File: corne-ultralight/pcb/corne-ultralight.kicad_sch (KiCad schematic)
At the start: 110 parts, among them J2 OLED, J7 OLED, SW1 SW_PUSH, SW10 SW_PUSH, SW11 SW_PUSH, SW12 SW_PUSH, SW13 SW_PUSH, SW14 SW_PUSH, SW15 SW_PUSH, SW16 SW_PUSH, SW17 SW_PUSH, SW18 SW_PUSH, SW19 SW_PUSH, SW2 SW_PUSH, SW20 SW_PUSH, SW21 SW_PUSH, SW22 SW_PUSH, SW23 SW_PUSH, SW24 SW_PUSH, SW25 SW_PUSH, SW26 SW_PUSH, SW27 SW_PUSH, SW28 SW_PUSH, SW29 SW_PUSH, SW3 SW_PUSH, SW30 SW_PUSH, SW31 SW_PUSH, SW32 SW_PUSH, SW33 SW_PUSH, SW34 SW_PUSH, SW35 SW_PUSH, SW36 SW_PUSH, SW37 SW_PUSH, SW38 SW_PUSH, SW39 SW_PUSH, SW4 SW_PUSH, SW40 SW_PUSH, SW41 SW_PUSH, SW42 SW_PUSH, SW5 SW_PUSH, SW6 SW_PUSH, SW7 SW_PUSH, SW8 SW_PUSH, SW9 SW_PUSH, U1 ProMicro, U2 ProMicro

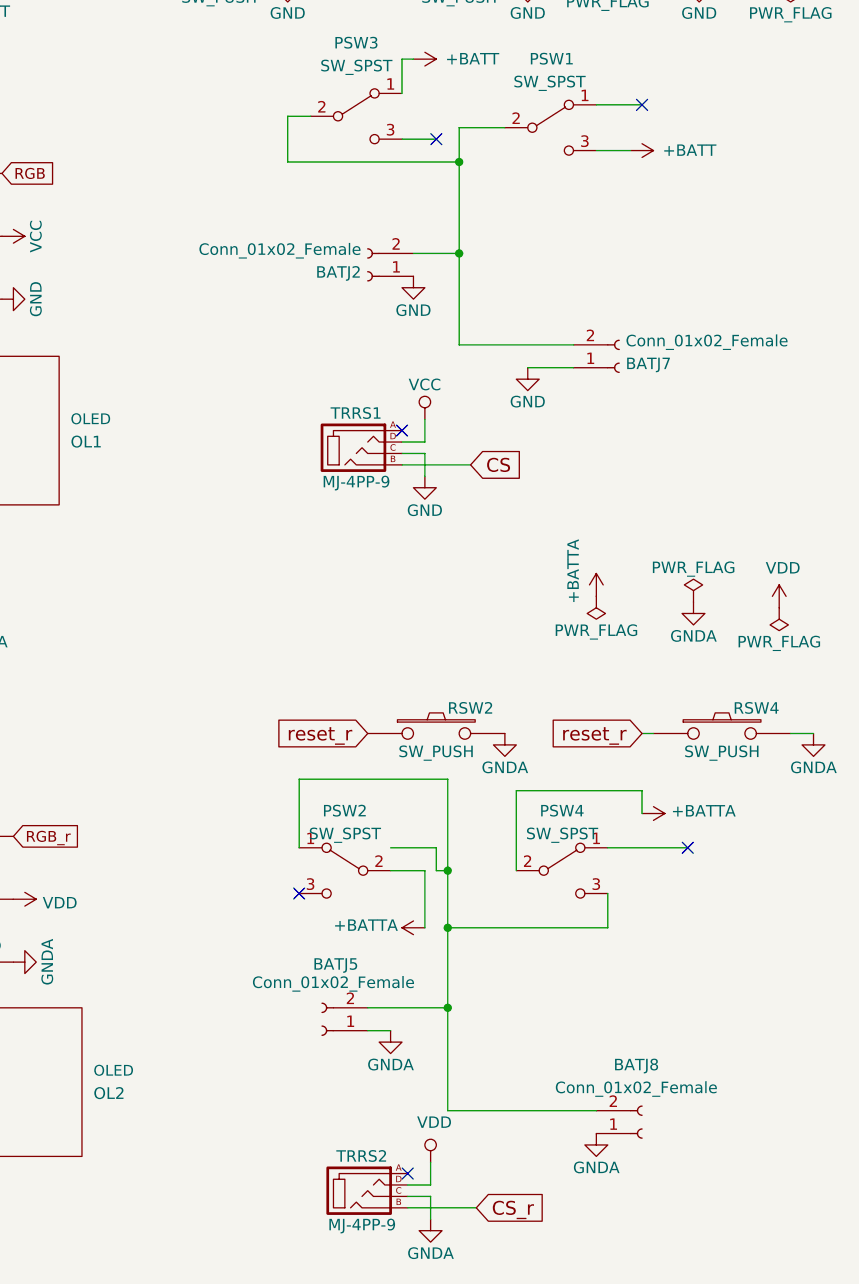
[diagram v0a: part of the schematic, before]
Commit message: Rerouting
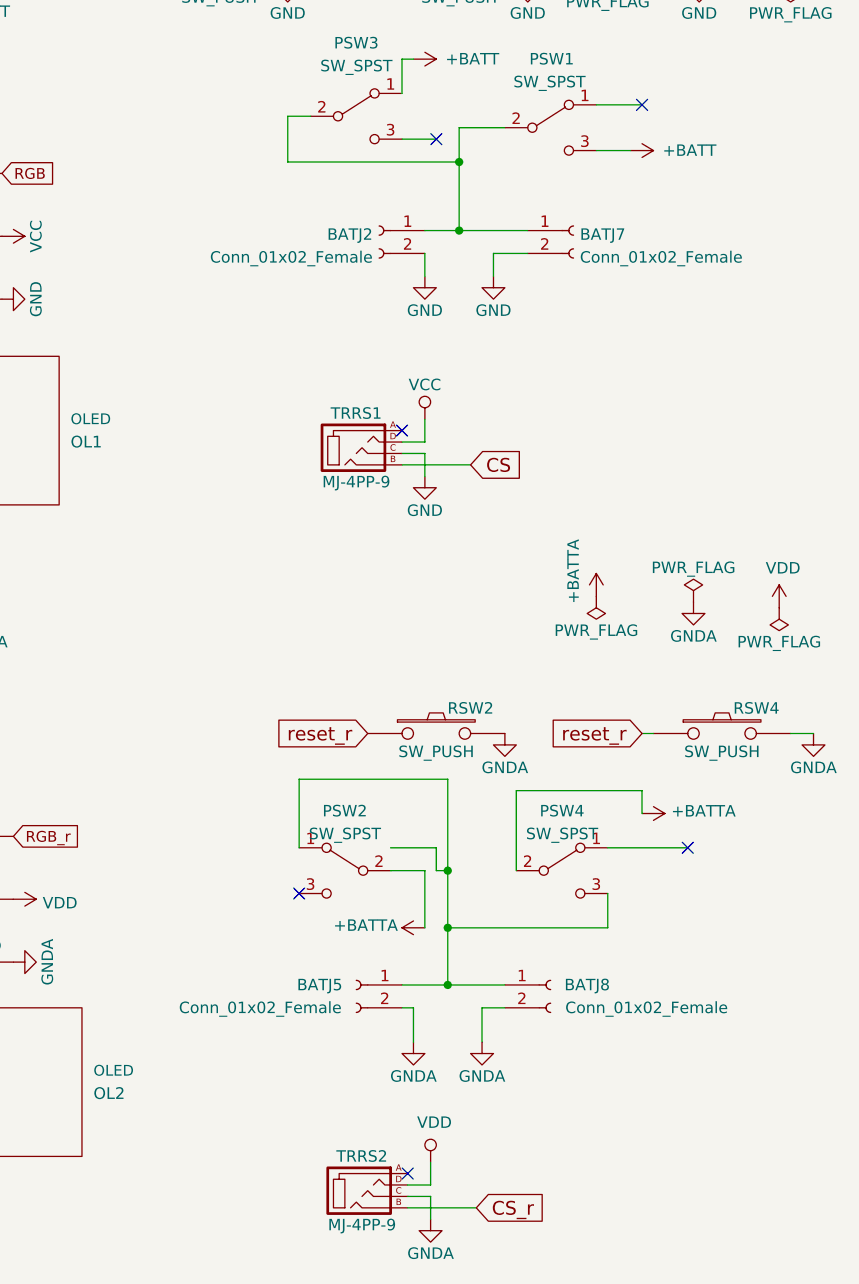
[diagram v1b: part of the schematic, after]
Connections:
- net GND: now also BATJ2.2 (Pin_2), BATJ7.2 (Pin_2); no longer BATJ2.1 (Pin_1), BATJ7.1 (Pin_1)
- net GNDA: now also BATJ5.2 (Pin_2), BATJ8.2 (Pin_2); no longer BATJ5.1 (Pin_1), BATJ8.1 (Pin_1)
- net at PSW2.1 (A), PSW4.3 (C): now also BATJ5.1 (Pin_1), BATJ8.1 (Pin_1); no longer BATJ5.2 (Pin_2), BATJ8.2 (Pin_2)
- net at PSW1.2 (B), PSW3.2 (B): now also BATJ2.1 (Pin_1), BATJ7.1 (Pin_1); no longer BATJ2.2 (Pin_2), BATJ7.2 (Pin_2)
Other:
- moved on the sheet: BATJ2, BATJ5, BATJ7, BATJ8

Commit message: Tons of improvements
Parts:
- PSW1, PSW2, PSW3, PSW4: footprint Button_Switch_SMD:SW_SPDT_PCM12 -> JxComponents:SW_SPDT_PCM12_JX
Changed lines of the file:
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@@
 			)
 		)
-		(property "Footprint" "Button_Switch_SMD:SW_SPDT_PCM12"
+		(property "Footprint" "JxComponents:SW_SPDT_PCM12_JX"
 			(at 252.73 35.56 0)
 			(effects
@@
 			)
 		)
-		(property "Footprint" "Button_Switch_SMD:SW_SPDT_PCM12"
+		(property "Footprint" "JxComponents:SW_SPDT_PCM12_JX"
 			(at 229.87 118.11 0)
 			(effects
@@
 			)
 		)
-		(property "Footprint" "Button_Switch_SMD:SW_SPDT_PCM12"
+		(property "Footprint" "JxComponents:SW_SPDT_PCM12_JX"
 			(at 254 118.11 0)
 			(effects
@@
 			)
 		)
-		(property "Footprint" "Button_Switch_SMD:SW_SPDT_PCM12"
+		(property "Footprint" "JxComponents:SW_SPDT_PCM12_JX"
 			(at 231.14 34.29 0)
 			(effects
